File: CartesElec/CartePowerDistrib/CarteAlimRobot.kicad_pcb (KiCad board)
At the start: 2 copper layers, 69 x 64 mm, 20 parts, among them J10 Conn_01x03_Male, J11 Conn_01x02_Male, J3 Screw_Terminal_01x02, J4 Screw_Terminal_01x02, J5 Screw_Terminal_01x02, J6 Screw_Terminal_01x02, J7 Screw_Terminal_01x02, J8 Screw_Terminal_01x02, J9 Conn_01x03_Male, Q1 IRF540N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

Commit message: Mise à jour du PCB + début d'optimisation
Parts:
- removed J11: Conn_01x02_Male, Connector_JST:JST_XH_B2B-XH-AM_1x02_P2.50mm_Vertical
- removed the REF** at (110.0, 100.0)
- removed the REF** at (114.0, 139.0)
- removed the REF** at (60.0, 139.0)
- added G***: LOGO, logo:logo, B.Cu at (78.0, 111.5)
- added G***: LOGO, logo:logo, F.Cu at (69.0, -16.0)
- added G***: LOGO, logo:logo, F.Cu at (94.0, 104.0)
- added REF**: MountingHole_3.2mm_M3, MountingHole:MountingHole_3.2mm_M3, F.Cu at (57.0, 140.5)
- added REF**: MountingHole_3.2mm_M3, MountingHole:MountingHole_3.2mm_M3, F.Cu at (112.0, 98.0)
- added REF**: MountingHole_3.2mm_M3, MountingHole:MountingHole_3.2mm_M3, F.Cu at (112.0, 140.5)
- J10: value Conn_01x03_Male -> Conn_01x04_Male; footprint Connector_JST:JST_EH_B3B-EH-A_1x03_P2.50mm_Vertical -> Connector_JST:JST_XH_B4B-XH-AM_1x04_P2.50mm_Vertical
- moved R1 18.4 mm to (99.0, 114.0), turned to 270 degrees
- moved J3 12.8 mm to (102.5, 99.0)
- moved R2 12.5 mm to (84.0, 114.0), turned to 270 degrees
- moved J9 11.5 mm to (89.0, 112.0), turned to 0 degrees
- moved Q1 11.4 mm to (74.0, 126.0), turned to 0 degrees
- moved J10 11.4 mm to (86.0, 124.0), turned to 0 degrees
- moved J6 11.2 mm to (102.0, 129.0)
- moved J7 10.1 mm to (89.0, 99.0)
- moved J1 9.10 mm to (74.0, 99.0)
- moved REF** 8.25 mm to (57.0, 98.0)
- moved U1 6.06 mm to (60.0, 114.0)
- moved C2 4.56 mm to (90.0, 120.0), turned to 180 degrees
- renumbered ArrêtUrgence to J1, BatterieGND to J2
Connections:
- J10 pad 1: GND -> SignalPowerOn
- J10 pad 2: +5V -> GND
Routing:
- net GND: track 103.5 -> 73.5 mm
- net +12V: track 159.6 -> 140.0 mm
- net GND_P: track 138.9 -> 126.0 mm
- net +5V: track 58.8 -> 68.5 mm, vias 2 -> 0
- net Net-(J1-Pad1): track 36.1 -> 29.7 mm
- net SignalPowerOn: track 24.3 -> 28.5 mm
- net Net-(J9-Pad3): track 6.89 -> 5.45 mm
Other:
- board size 69 x 64 mm -> 61.5 x 51 mm
- board text added: "12V"
- board text added: "Arrêt d'urgence"
- board text added: "Batterie GND"
- board text added: "Carte d'alimentation"
- board text added: "GND"
- board text added: "V @ ENAC"

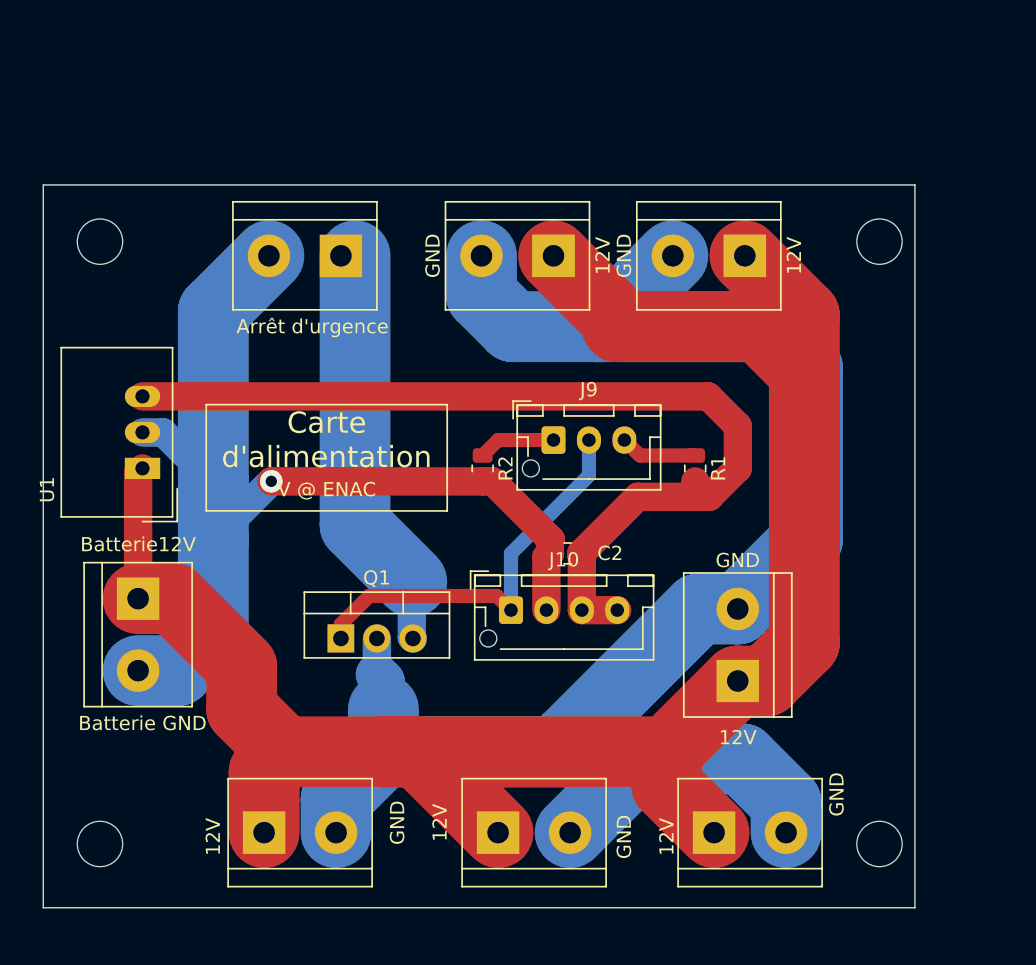
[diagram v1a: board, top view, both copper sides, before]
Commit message: Optimisation d'espace sur la carte d'alim
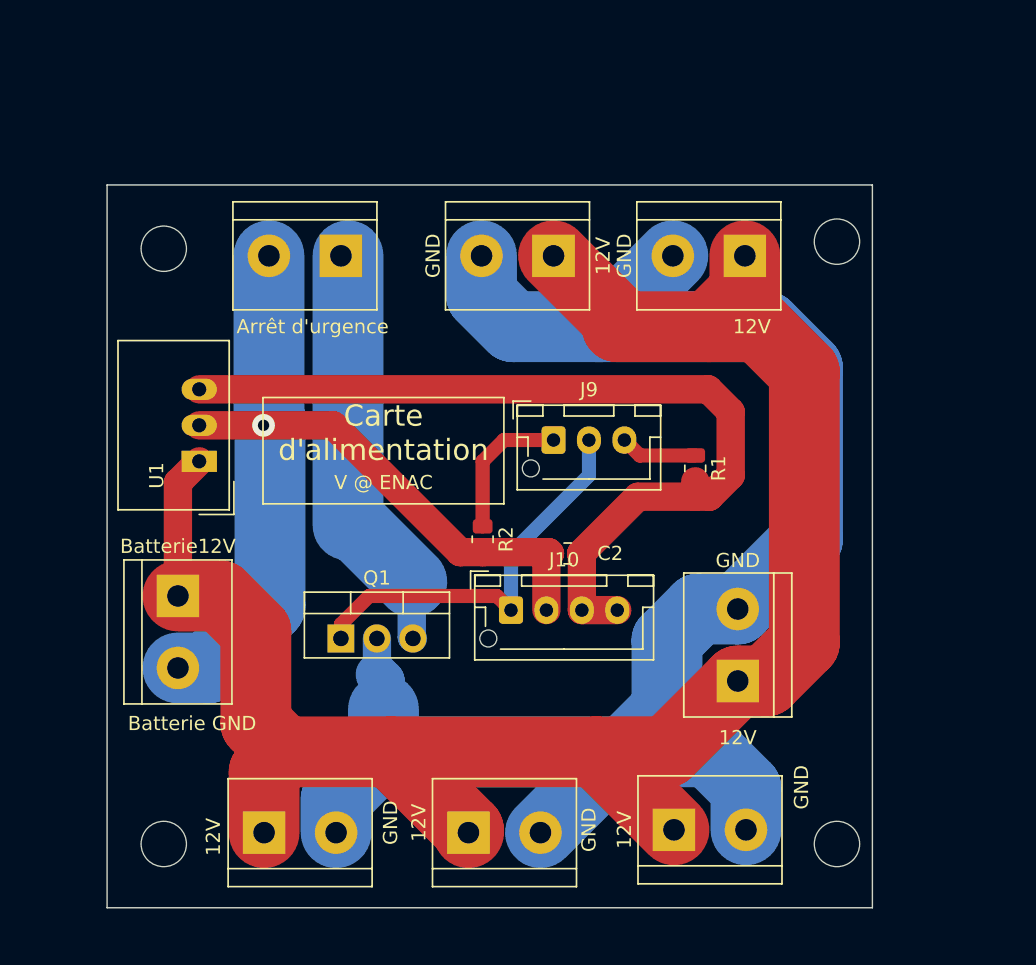
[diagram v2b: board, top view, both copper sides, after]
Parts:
- removed the REF** at (112.0, 98.0)
- removed the REF** at (112.0, 140.5)
- added REF**: MountingHole_3.2mm_M3, MountingHole:MountingHole_3.2mm_M3, F.Cu at (109.0, 98.0)
- added REF**: MountingHole_3.2mm_M3, MountingHole:MountingHole_3.2mm_M3, F.Cu at (109.0, 140.5)
- moved R2 5.00 mm to (84.0, 119.0)
- moved REF** 4.53 mm to (61.5, 98.5)
- moved REF** 4.50 mm to (61.5, 140.5)
- moved U1 4.03 mm to (64.0, 113.5)
- moved J4 2.84 mm to (97.5, 139.5)
- moved J2 2.82 mm to (62.5, 123.0)
- moved J8 2.09 mm to (83.0, 139.7)
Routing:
- net GND: track 73.5 -> 65.6 mm
- net +12V: track 140.0 -> 134.4 mm
- net Net-(J9-Pad1): track 5.45 -> 10.2 mm
- net +5V: track 68.5 -> 64.6 mm
- net GND_P: track 126.0 -> 122.8 mm
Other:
- board size 61.5 x 51 mm -> 54 x 51 mm

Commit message: fin de la carte d'alim
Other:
- board text added: "JLCJLCJLCJLC"
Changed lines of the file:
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@@
-(kicad_pcb (version 20171130) (host pcbnew 5.1.7-a382d34a8~88~ubuntu18.04.1)
+(kicad_pcb (version 20171130) (host pcbnew "(5.1.0)-1")
   (general
     (thickness 1.6)
-    (drawings 25)
+    (drawings 26)
     (tracks 94)
     (zones 0)
@@
     (34 B.Paste user)
     (35 F.Paste user)
-    (36 B.SilkS user hide)
-    (37 F.SilkS user)
+    (36 B.SilkS user)
+    (37 F.SilkS user hide)
     (38 B.Mask user)
     (39 F.Mask user)
@@
   )
   (setup
-    (last_trace_width 1)
+    (last_trace_width 0.25)
     (user_trace_width 1)
     (user_trace_width 2)
@@
     (pad_to_mask_clearance 0)
     (aux_axis_origin 0 0)
-    (visible_elements FFFFFF7F)
+    (visible_elements 7FFFFFFF)
     (pcbplotparams
       (layerselection 0x010fc_ffffffff)
-      (usegerberextensions false)
-      (usegerberattributes true)
-      (usegerberadvancedattributes true)
-      (creategerberjobfile true)
+      (usegerberextensions true)
+      (usegerberattributes false)
+      (usegerberadvancedattributes false)
+      (creategerberjobfile false)
       (excludeedgelayer true)
       (linewidth 0.100000)
-      (plotframeref false)
+      (plotframeref true)
       (viasonmask false)
       (mode 1)
@@
       (plotinvisibletext false)
       (padsonsilk false)
-      (subtractmaskfromsilk false)
+      (subtractmaskfromsilk true)
       (outputformat 1)
       (mirror false)
-      (drillshape 1)
+      (drillshape 0)
       (scaleselection 1)
-      (outputdirectory ""))
+      (outputdirectory "gerber/"))
   )
   (net 0 "")
@@
     )
   )
+  (gr_text JLCJLCJLCJLC (at 86.36 130.81) (layer B.SilkS)
+    (effects (font (size 1 1) (thickness 0.15)) (justify mirror))
+  )
   (gr_line (start 68.5 116.5) (end 68.5 109) (layer F.SilkS) (width 0.12))

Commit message: Carte Alim V2
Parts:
- removed the G*** at (69.0, -16.0)
- removed Q1: IRF540N, Package_TO_SOT_THT:TO-220-3_Vertical
- added R3: R, Resistor_SMD:R_0805_2012Metric, F.Cu at (92.0, 118.0)
- added R4: R, Resistor_SMD:R_0805_2012Metric, F.Cu at (79.0, 124.0)
- added R5: R, Resistor_SMD:R_0805_2012Metric, F.Cu at (79.0, 127.0)
- added U2: ASSR-1218, Package_SO:SO-4_4.4x3.6mm_P2.54mm, F.Cu at (72.0, 125.0)
- J10: value Conn_01x04_Male -> Conn_01x02_Male; footprint Connector_JST:JST_XH_B4B-XH-AM_1x04_P2.50mm_Vertical -> Connector_JST:JST_EH_B2B-EH-A_1x02_P2.50mm_Vertical
- J8: value Screw_Terminal_01x02 -> USB_A; footprint TerminalBlock:TerminalBlock_bornier-2_P5.08mm -> Connector_USB:USB_A_Molex_67643_Horizontal
- J9: value Conn_01x03_Male -> (none)
- moved J7 41.3 mm to (84.0, 140.0), turned to 0 degrees
- moved J8 32.0 mm to (89.5, 108.4), turned to 180 degrees
- moved J6 11.8 mm to (105.0, 117.5)
- moved J4 10.2 mm to (105.0, 132.5), turned to 90 degrees
- moved J10 9.90 mm to (79.0, 131.0)
- moved J9 9.17 mm to (82.5, 118.5)
- moved C2 7.62 mm to (87.0, 113.0)
- moved R2 6.00 mm to (83.0, 113.1), turned to 90 degrees
- moved R1 5.66 mm to (95.0, 118.0), turned to 90 degrees
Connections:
- J1 pad 2: GND -> +12V
- J3 pad 1: +12V -> 12V_P
- J3 pad 2: GND_P -> GND
- J4 pad 1: +12V -> 12V_P
- J4 pad 2: GND_P -> GND
- J5 pad 1: +12V -> 12V_P
- J5 pad 2: GND_P -> GND
- J6 pad 1: +12V -> 12V_P
- J6 pad 2: GND_P -> GND
- J7 pad 1: +12V -> 12V_P
- J7 pad 2: GND_P -> GND
- J8 pad 1: +12V -> +5V
- J8 pad 2: GND_P -> unconnected-(J8-Pad2)
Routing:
- net GND_P: track 122.8 -> 0.00 mm
- net GND: track 65.6 -> 178.0 mm, vias 1 -> 0
- net 12V_P: track 0.00 -> 107.6 mm
- net +12V: track 134.4 -> 30.9 mm
- net +5V: track 64.6 -> 45.0 mm
- net SignalPowerOn: track 28.5 -> 15.1 mm
- net unconnected-(J8-Pad5): track 0.00 -> 13.1 mm
- net Net-(R4-Pad2): track 0.00 -> 6.24 mm
- net Net-(J9-Pad1): track 10.2 -> 4.68 mm
- net Net-(J1-Pad1): track 29.7 -> 27.2 mm
- net Net-(J9-Pad3): track 5.45 -> 7.68 mm
- added copper zone on F.Cu, net +12V
- added copper zone on F.Cu, net 12V_P
- added copper zone on B.Cu, net GND
- added copper zone on F.Cu, net Net-(J1-Pad1)
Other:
- net class Default removed
- board text added: "Carte d'alimentation Version 2"
- board text added: "by V @ ENAC"
- board text removed: "Carte d'alimentation"
- board text removed: "JLCJLCJLCJLC"
- board text removed: "V @ ENAC"

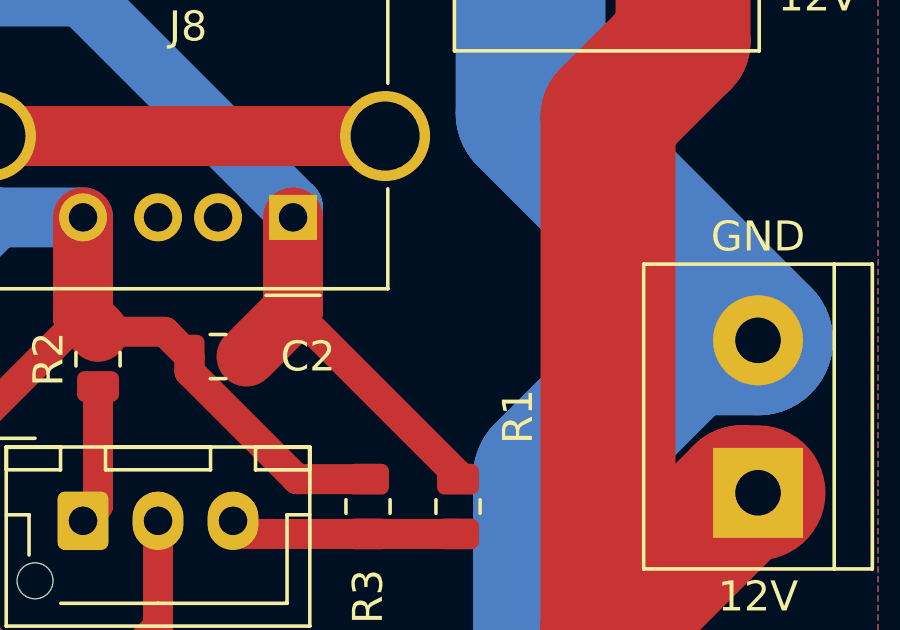
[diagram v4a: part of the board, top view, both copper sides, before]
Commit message: Carte Alim V2.1\nAjout d'un interrupteur pour la RaspbPi
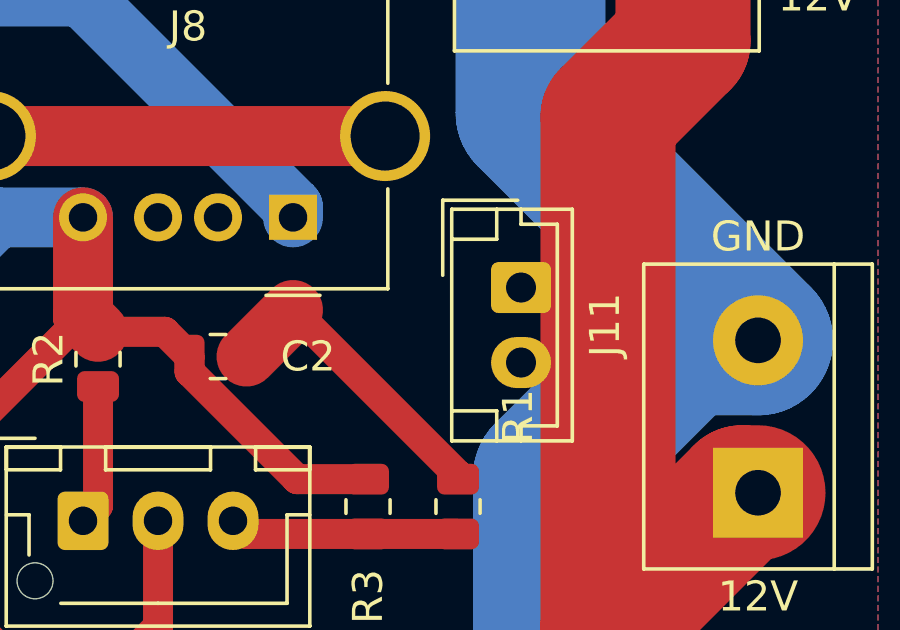
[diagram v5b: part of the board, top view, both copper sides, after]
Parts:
- added J11: Conn_01x02_Male, Connector_JST:JST_EH_B2B-EH-A_1x02_P2.50mm_Vertical, F.Cu at (97.1, 110.7)
- J9: value (none) -> Conn_01x03_Male
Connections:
- J8 pad 1: +5V -> Net-(J8-Pad1)
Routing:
- net +5V: track 45.0 -> 41.9 mm
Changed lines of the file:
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@@
   (net 11 "unconnected-(J8-Pad5)")
   (net 12 "Net-(R4-Pad2)")
+  (net 13 "Net-(J8-Pad1)")
   (footprint "Capacitor_SMD:C_0805_2012Metric" (layer "F.Cu")
     (at 87 113 180)
@@
       (effects (font (size 1 1) (thickness 0.15)))
     )
-    (fp_text value " " (at 2.5 4.6) (layer "F.Fab")
+    (fp_text value "Conn_01x03_Male" (at 2.5 4.6) (layer "F.Fab")
       (effects (font (size 1 1) (thickness 0.15)))
     )
@@
     (fp_line (start -3.05 12.69) (end -3.05 -2.27) (layer "F.Fab") (width 0.1))
     (pad "1" thru_hole rect (at 0 0 180) (size 1.6 1.5) (drill 0.95) (layers *.Cu *.Mask)
-      (net 1 "+5V") (pinfunction "VBUS") (pintype "power_in"))
+      (net 13 "Net-(J8-Pad1)") (pinfunction "VBUS") (pintype "power_in"))
     (pad "2" thru_hole circle (at 2.5 0 180) (size 1.6 1.6) (drill 0.95) (layers *.Cu *.Mask)
       (net 9 "unconnected-(J8-Pad2)") (pinfunction "D-") (pintype "bidirectional+no_connect"))
@@
   )
   (footprint "Connector_JST:JST_EH_B2B-EH-A_1x02_P2.50mm_Vertical" (layer "F.Cu")
+    (at 97.1 110.7 -90)
+    (descr "JST EH series connector, B2B-EH-A (http://www.jst-mfg.com/product/pdf/eng/eEH.pdf), generated with kicad-footprint-generator")
+    (tags "connector JST EH vertical")
+    (property "Sheetfile" "CarteAlimRobot.kicad_sch")
+    (property "Sheetname" "")
+    (attr through_hole)
+    (fp_text reference "J11" (at 1.25 -2.8 90) (layer "F.SilkS")
+      (effects (font (size 1 1) (thickness 0.15)))
+    )
+    (fp_text value "Conn_01x02_Male" (at 1.25 3.4 90) (layer "F.Fab")
+      (effects (font (size 1 1) (thickness 0.15)))
+    )
+    (fp_text user "${REFERENCE}" (at 1.25 1.5 90) (layer "F.Fab")
+      (effects (font (size 1 1) (thickness 0.15)))
+    )
+    (fp_line (start -2.11 0) (end -2.11 -1.21) (layer "F.SilkS") (width 0.12))
+    (fp_line (start 5.11 2.31) (end 5.11 -1.71) (layer "F.SilkS") (width 0.12))
+    (fp_line (start -2.61 0.81) (end -1.61 0.81) (layer "F.SilkS") (width 0.12))
+    (fp_line (start 4.11 0.81) (end 4.11 2.31) (layer "F.SilkS") (width 0.12))
+    (fp_line (start -2.11 -1.21) (end 4.61 -1.21) (layer "F.SilkS") (width 0.12))
+    (fp_line (start -2.61 -1.71) (end -2.61 2.31) (layer "F.SilkS") (width 0.12))
+    (fp_line (start -2.91 2.61) (end -0.41 2.61) (layer "F.SilkS") (width 0.12))
+    (fp_line (start 5.11 0.81) (end 4.11 0.81) (layer "F.SilkS") (width 0.12))
+    (fp_line (start -1.61 0.81) (end -1.61 2.31) (layer "F.SilkS") (width 0.12))
+    (fp_line (start 4.61 0) (end 5.11 0) (layer "F.SilkS") (width 0.12))
+    (fp_line (start 4.61 -1.21) (end 4.61 0) (layer "F.SilkS") (width 0.12))
+    (fp_line (start -2.91 0.11) (end -2.91 2.61) (layer "F.SilkS") (width 0.12))
+    (fp_line (start -2.61 2.31) (end 5.11 2.31) (layer "F.SilkS") (width 0.12))
+    (fp_line (start 5.11 -1.71) (end -2.61 -1.71) (layer "F.SilkS") (width 0.12))
+    (fp_line (start -2.61 0) (end -2.11 0) (layer "F.SilkS") (width 0.12))
+    (fp_line (start 5.5 -2.1) (end -3 -2.1) (layer "F.CrtYd") (width 0.05))
+    (fp_line (start -3 -2.1) (end -3 2.7) (layer "F.CrtYd") (width 0.05))
+    (fp_line (start -3 2.7) (end 5.5 2.7) (layer "F.CrtYd") (width 0.05))
+    (fp_line (start 5.5 2.7) (end 5.5 -2.1) (layer "F.CrtYd") (width 0.05))
+    (fp_line (start 5 -1.6) (end -2.5 -1.6) (layer "F.Fab") (width 0.1))
+    (fp_line (start -2.5 2.2) (end 5 2.2) (layer "F.Fab") (width 0.1))
+    (fp_line (start 5 2.2) (end 5 -1.6) (layer "F.Fab") (width 0.1))
+    (fp_line (start -2.91 2.61) (end -0.41 2.61) (layer "F.Fab") (width 0.1))
+    (fp_line (start -2.91 0.11) (end -2.91 2.61) (layer "F.Fab") (width 0.1))
+    (fp_line (start -2.5 -1.6) (end -2.5 2.2) (layer "F.Fab") (width 0.1))
+    (pad "1" thru_hole roundrect (at 0 0 270) (size 1.7 2) (drill 1) (layers *.Cu *.Mask) (roundrect_rratio 0.147059)
+      (net 13 "Net-(J8-Pad1)") (pinfunction "Pin_1") (pintype "passive"))
+    (pad "2" thru_hole oval (at 2.5 0 270) (size 1.7 2) (drill 1) (layers *.Cu *.Mask)
+      (net 1 "+5V") (pinfunction "Pin_2") (pintype "passive"))
+    (model "${KICAD6_3DMODEL_DIR}/Connector_JST.3dshapes/JST_EH_B2B-EH-A_1x02_P2.50mm_Vertical.wrl"
+      (offset (xyz 0 0 0))
+      (scale (xyz 1 1 1))
+      (rotate (xyz 0 0 0))
+    )
+  )
+  (footprint "Connector_JST:JST_EH_B2B-EH-A_1x02_P2.50mm_Vertical" (layer "F.Cu")
     (at 79 131)
     (descr "JST EH series connector, B2B-EH-A (http://www.jst-mfg.com/product/pdf/eng/eEH.pdf), generated with kicad-footprint-generator")
@@
   )
   (segment (start 95 116.95) (end 89.5 111.45) (width 1) (layer "F.Cu") (net 1))
-  (segment (start 89.5 108.36) (end 89.5 111.45) (width 2) (layer "F.Cu") (net 1))
   (segment (start 89.5 111.45) (end 87.95 113) (width 2) (layer "F.Cu") (net 1))
   (segment (start 95 117.0875) (end 95 116.95) (width 1) (layer "F.Cu") (net 1))
